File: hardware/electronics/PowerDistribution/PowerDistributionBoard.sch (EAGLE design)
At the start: 82 parts, among them IC1 LM556D, IC2 74AHC1G02DBV, IC3 74AHC1G02DBV, K1 EC2-12TNU, U1 IPS6041G, U2 IPS6041G, U3 V_REG_317SMD

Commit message: Control board BoM complete
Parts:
- ARM-BUTTON, STOP-BUTTON: PARTNO (none) -> 0705550037
- AUX-PWR, MAIN-RELAY, MOTOR-RELAY: PARTNO (none) -> 0705550036
- AUX1, AUX2, CTRL, HORN, MAIN, MOTOR: PARTNO (none) -> M2012LL1W01
- AUX1-PWR, AUX2-PWR, CTL-PWR, HORN-PWR, PWR-IN: PARTNO (none) -> 1751248
- C1, C3: PARTNO (none) -> CL10B103KB8NCNC
- LED1, LED10, LED2, LED3, LED4, LED5, LED6, LED7, LED8, LED9: PARTNO (none) -> LG R971-KN-1
- PWR-STATE: PARTNO (none) -> 0705550039
- U1, U2: PARTNO (none) -> IPS6041GPBF

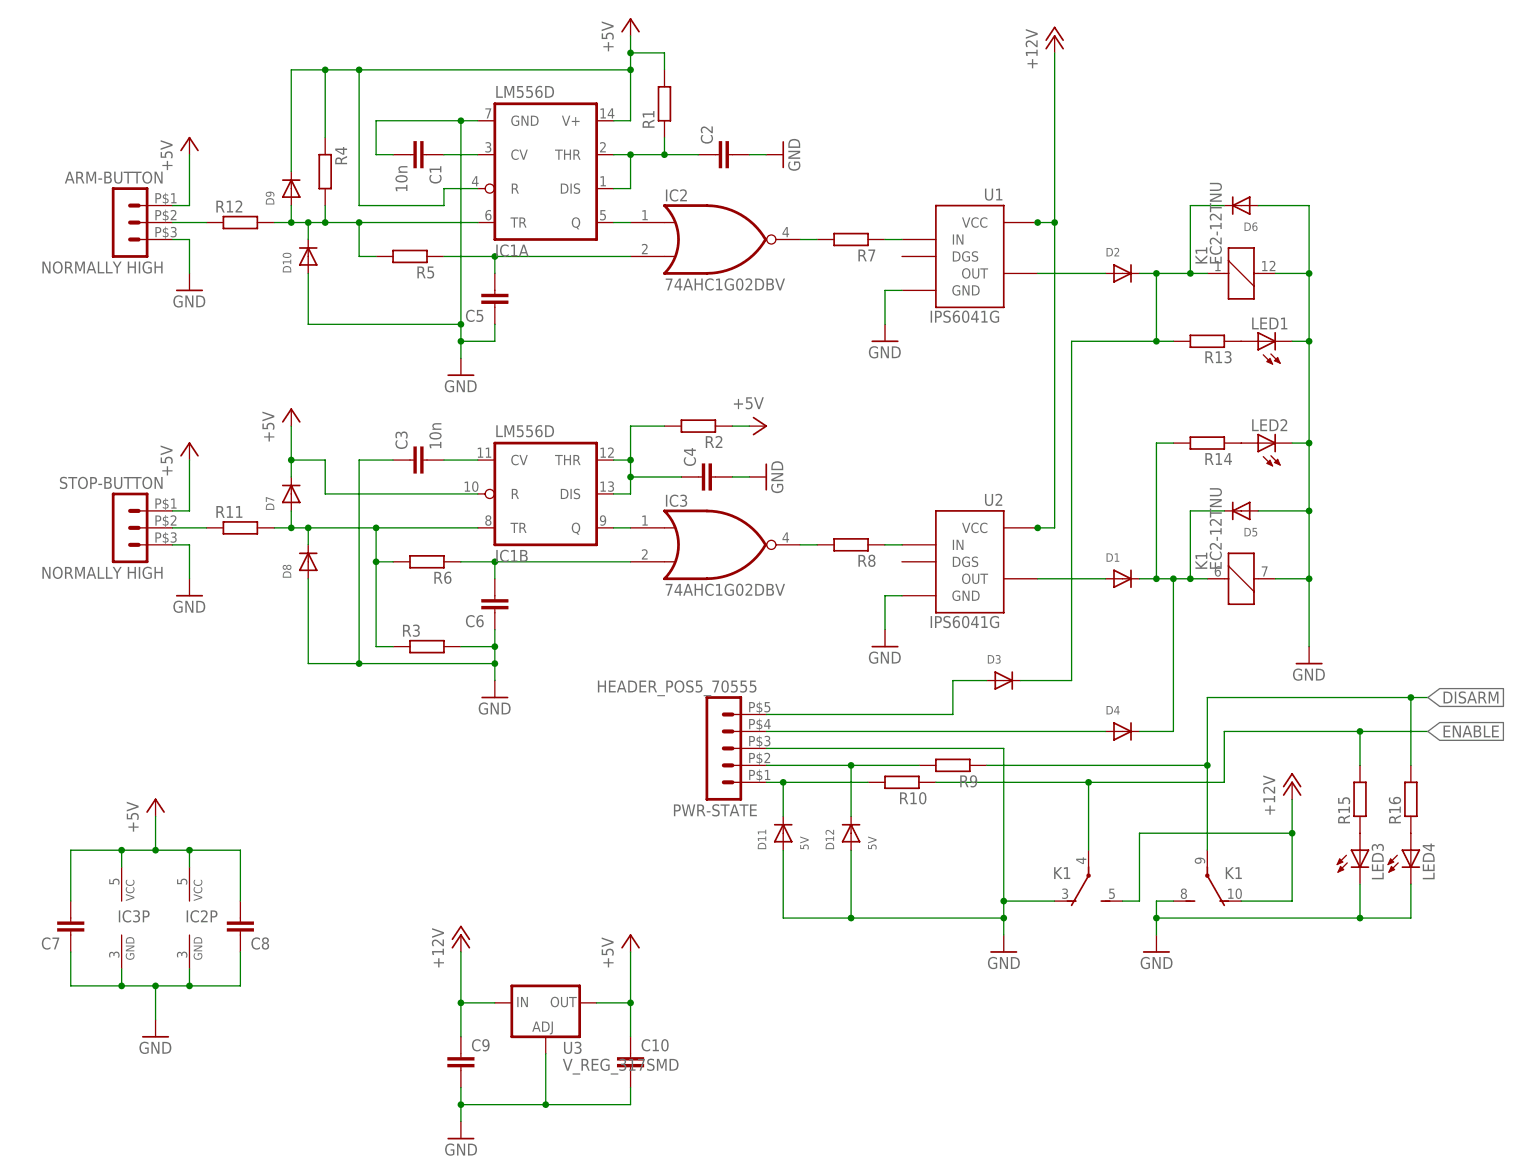
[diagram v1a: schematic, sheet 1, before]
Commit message: Fixed some issues with .gitignore and added some values and attributes to the power distribution board
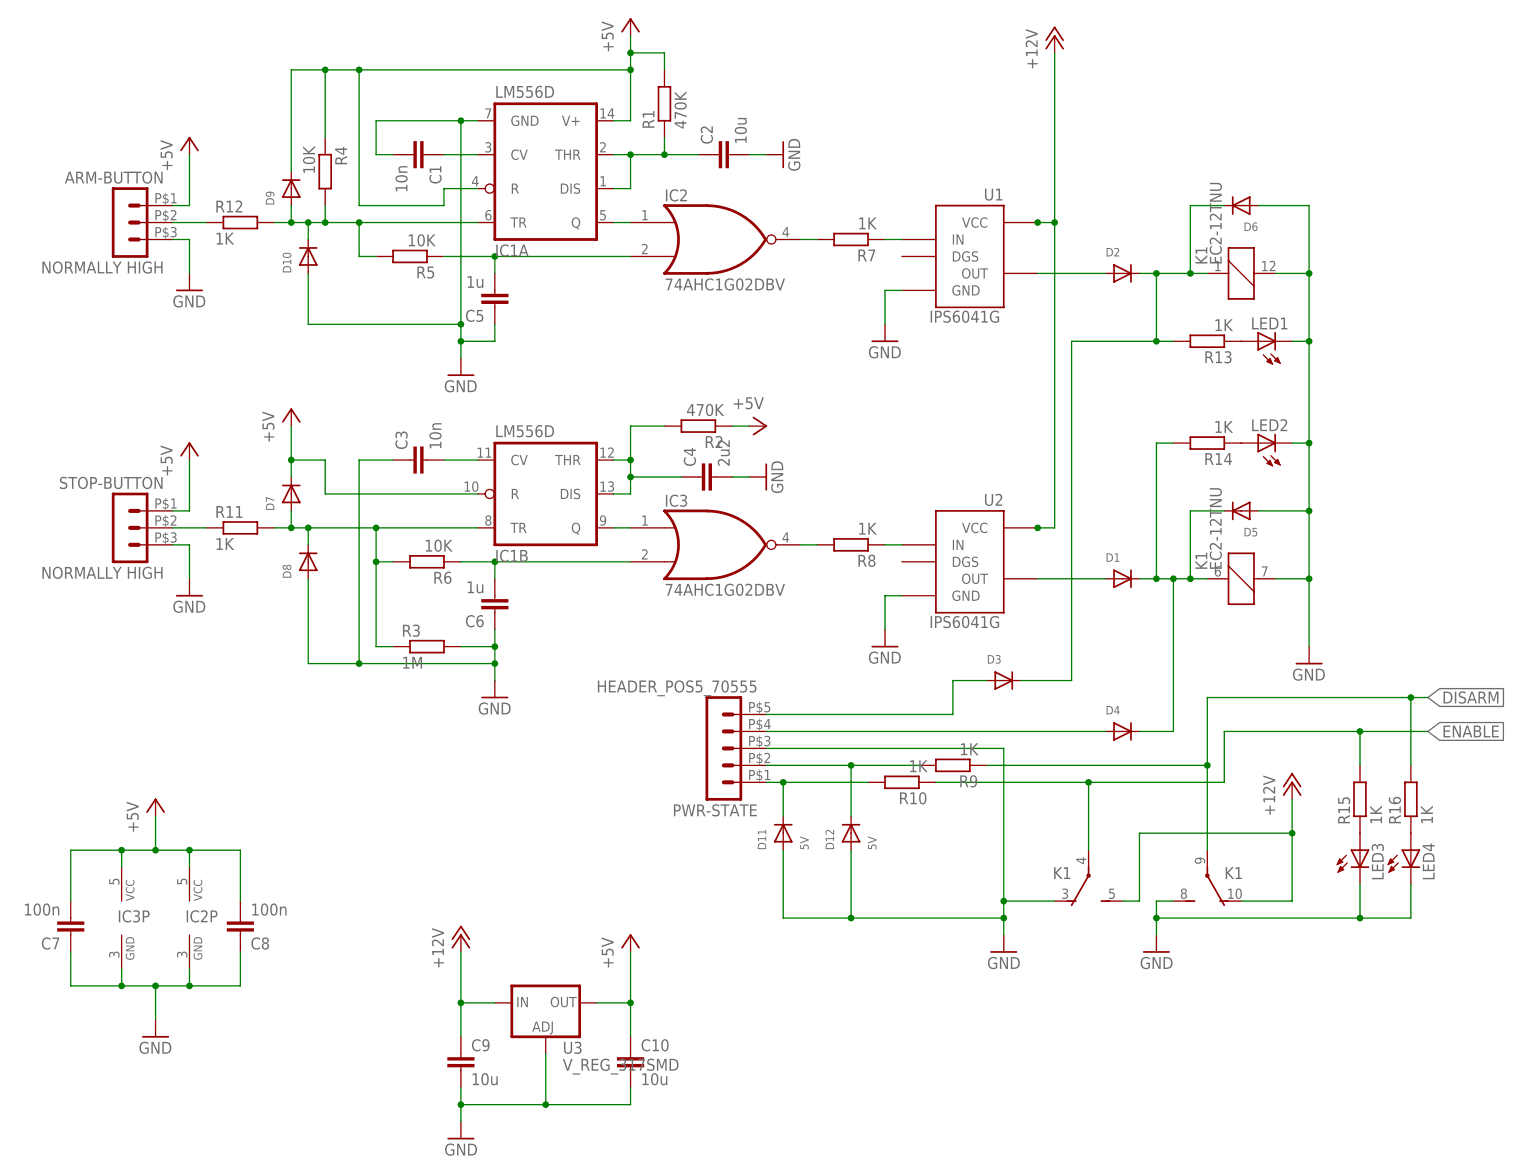
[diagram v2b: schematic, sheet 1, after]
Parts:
- C10, C9: value (none) -> 10u; PARTNO (none) -> C3216X5R1E106M
- C2: value (none) -> 10u; PARTNO (none) -> C1608JB1E106M080AC
- C4: value (none) -> 2u2; PARTNO (none) -> TMK107ABJ225KA-T
- C5, C6: value (none) -> 1u; PARTNO (none) -> UMK107BJ105KA-T
- C7, C8: value (none) -> 100n; PARTNO (none) -> CC0603ZRY5V9BB104
- D1, D10, D2, D3, D4, D5, D6, D7, D8, D9: PARTNO (none) -> CDBW140-G
- D11, D12: PARTNO (none) -> SMF5.0A
- H1, H2, H3, H4: BOM (none) -> EXCLUDE
- IC1: PARTNO (none) -> LM556CM
- IC2, IC3: PARTNO (none) -> SN74AHC1G02DBVR
- R1, R2: value (none) -> 470K; PARTNO (none) -> MCR03FZPEJ474
- R10, R11, R12, R13, R14, R15, R16, R17, R18, R19, R20, R21, R22, R7, R8, R9: value (none) -> 1K; PARTNO (none) -> RMCF0603FT1K00
- R3: value (none) -> 1M; PARTNO (none) -> MCT06030C1004FP500
- R4, R5, R6: value (none) -> 10K; PARTNO (none) -> RMCF0603FT10K0
- U3: PARTNO (none) -> NCP1117ST50T3G
